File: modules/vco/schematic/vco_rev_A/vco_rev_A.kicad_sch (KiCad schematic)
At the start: 0 parts

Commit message: fixed the lib path in the VCO project
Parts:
- added Q1: 2N2978, ProjectLib_Transient:TO-5-6, symbol ProjectLib_Transient:2N2978
- added R1: 68k, Resistor_THT:R_Axial_DIN0207_L6.3mm_D2.5mm_P10.16mm_Horizontal, symbol Device:R_US
- added U1: OP275, Package_DIP:DIP-8_W7.62mm_Socket_LongPads, symbol Amplifier_Operational:OP275
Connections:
- new net: Q1.1 (E1), Q1.5 (E2), R1.1
- new net: R1.2, U1.1

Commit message: updated the article
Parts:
- added C1: C, Capacitor_THT:C_Rect_L7.0mm_W2.0mm_P5.00mm, symbol Device:C
- added R2: 1M, Resistor_THT:R_Axial_DIN0207_L6.3mm_D2.5mm_P10.16mm_Horizontal, symbol Device:R_US
- added RV1: 2.2k, Potentiometer_THT:Potentiometer_Bourns_3296W_Vertical, symbol Device:R_Potentiometer_US
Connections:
- net at Q1.3 (C1): now also R2.2
- net GND: now reaches Q1.6 (B2)
- net at Q1.7 (C2): now also RV1.3
- new net: C1.2, RV1.1, RV1.2

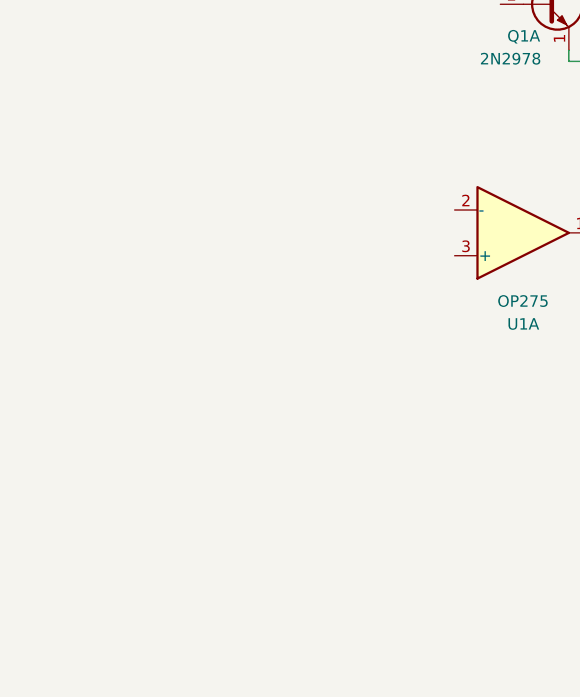
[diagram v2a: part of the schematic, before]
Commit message: added STM32 preliminary project for the VCO
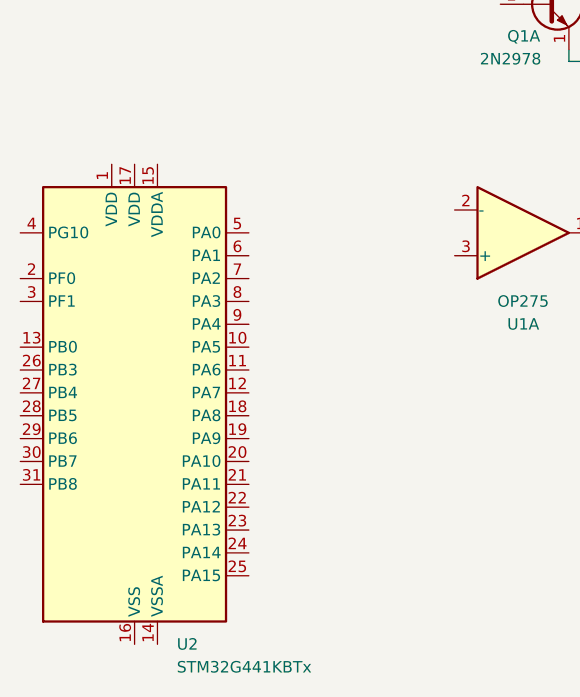
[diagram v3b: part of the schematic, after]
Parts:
- added U2: STM32G441KBTx, Package_QFP:LQFP-32_7x7mm_P0.8mm, symbol MCU_ST_STM32G4:STM32G441KBTx
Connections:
- new net: U2.16 (VSS), U2.32 (VSS)
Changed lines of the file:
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@@
+		)
+	)
+	(symbol
+		(lib_id "MCU_ST_STM32G4:STM32G441KBTx")
+		(at 87.63 194.31 0)
+		(unit 1)
+		(exclude_from_sim no)
+		(in_bom yes)
+		(on_board yes)
+		(dnp no)
+		(fields_autoplaced yes)
+		(property "Reference" "U2"
+			(at 92.3133 219.71 0)
+			(effects
+				(font
+					(size 1.27 1.27)
+				)
+				(justify left)
+			)
+		)
+		(property "Value" "STM32G441KBTx"
+			(at 92.3133 222.25 0)
+			(effects
+				(font
+					(size 1.27 1.27)
+				)
+				(justify left)
+			)
+		)
+		(property "Footprint" "Package_QFP:LQFP-32_7x7mm_P0.8mm"
+			(at 77.47 217.17 0)
+			(effects
+				(font
+					(size 1.27 1.27)
+				)
+				(justify right)
+				(hide yes)
+			)
+		)
+		(property "Datasheet" "https://www.st.com/resource/en/datasheet/stm32g441kb.pdf"
+			(at 87.63 194.31 0)
+			(effects
+				(font
+					(size 1.27 1.27)
+				)
+				(hide yes)
+			)
+		)
+		(property "Description" "STMicroelectronics Arm Cortex-M4 MCU, 128KB flash, 32KB RAM, 170 MHz, 1.71-3.6V, 26 GPIO, LQFP32"
+			(at 87.63 194.31 0)
+			(effects
+				(font
+					(size 1.27 1.27)
+				)
+				(hide yes)
+			)
+		)
+		(pin "2"
+		)
+		(pin "18"
+		)
+		(pin "20"
+		)
+		(pin "19"
+		)
+		(pin "3"
+		)
+		(pin "16"
+		)
+		(pin "32"
+		)
+		(pin "14"
+		)
+		(pin "10"
+		)
+		(pin "24"
+		)
+		(pin "8"
+		)
+		(pin "13"
+		)
+		(pin "11"
+		)
+		(pin "5"
+		)
+		(pin "12"
+		)
+		(pin "15"
+		)
+		(pin "29"
+		)
+		(pin "31"
+		)
+		(pin "4"
+		)
+		(pin "9"
+		)
+		(pin "23"
+		)
+		(pin "21"
+		)
+		(pin "26"
+		)
+		(pin "22"
+		)
+		(pin "27"
+		)
+		(pin "28"
+		)
+		(pin "7"
+		)
+		(pin "1"
+		)
+		(pin "17"
+		)
+		(pin "25"
+		)
+		(pin "30"
+		)
+		(pin "6"
+		)
+		(instances
+			(project ""
+				(path "/06df6441-3706-4d81-809c-6908b7c5817b"
+					(reference "U2")
+					(unit 1)
+				)
+			)
 		)
 	)
